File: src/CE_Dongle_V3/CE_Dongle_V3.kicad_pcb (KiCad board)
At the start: 4 copper layers, 44 x 44 mm, 106 parts, among them J1 USB_C_Receptacle_USB2.0_16P, J2 8P8C_LED_Shielded, J3 Conn_Coaxial, J4 Conn_02x05_Odd_Even, J5 Conn_01x02, Q1 AO3401A, Q2 AO3401A, Q3 BC817-40-7-F, Q4 BC817-40-7-F, Q5 BC817-40-7-F, U1 ESP32-C6, U10 TMUX1208QRSVRQ1, U11 TPS70950DBVR, U2 SP3485, U3 W25Q64JWUUIQ, U4 TPS54302DDCR, U5 PCF8574RGTR(UMW), U6 PCF8574RGTR(UMW), U7 TMUX1208QRSVRQ1, U8 TMUX1208QRSVRQ1, U9 TMUX1208QRSVRQ1, Y1 40MHz

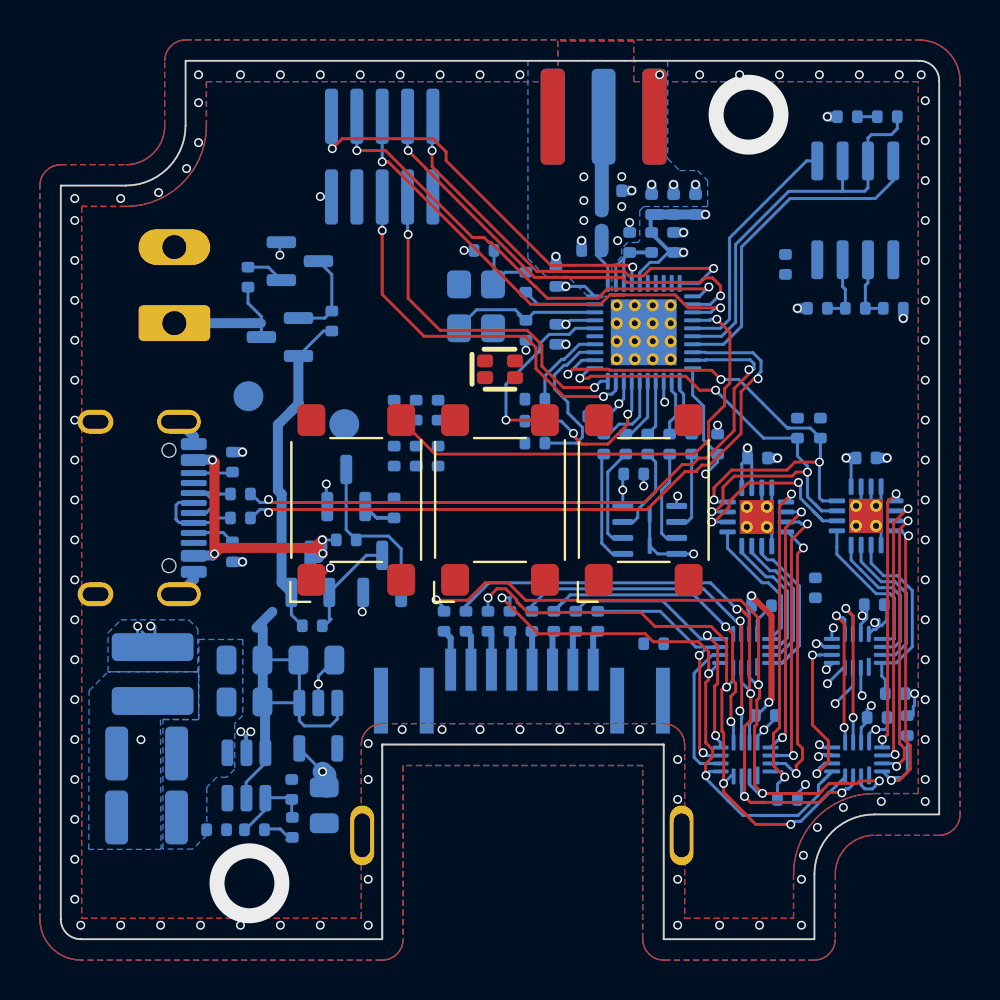
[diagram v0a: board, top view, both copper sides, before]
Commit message: layout cont. corrected some wrong net names
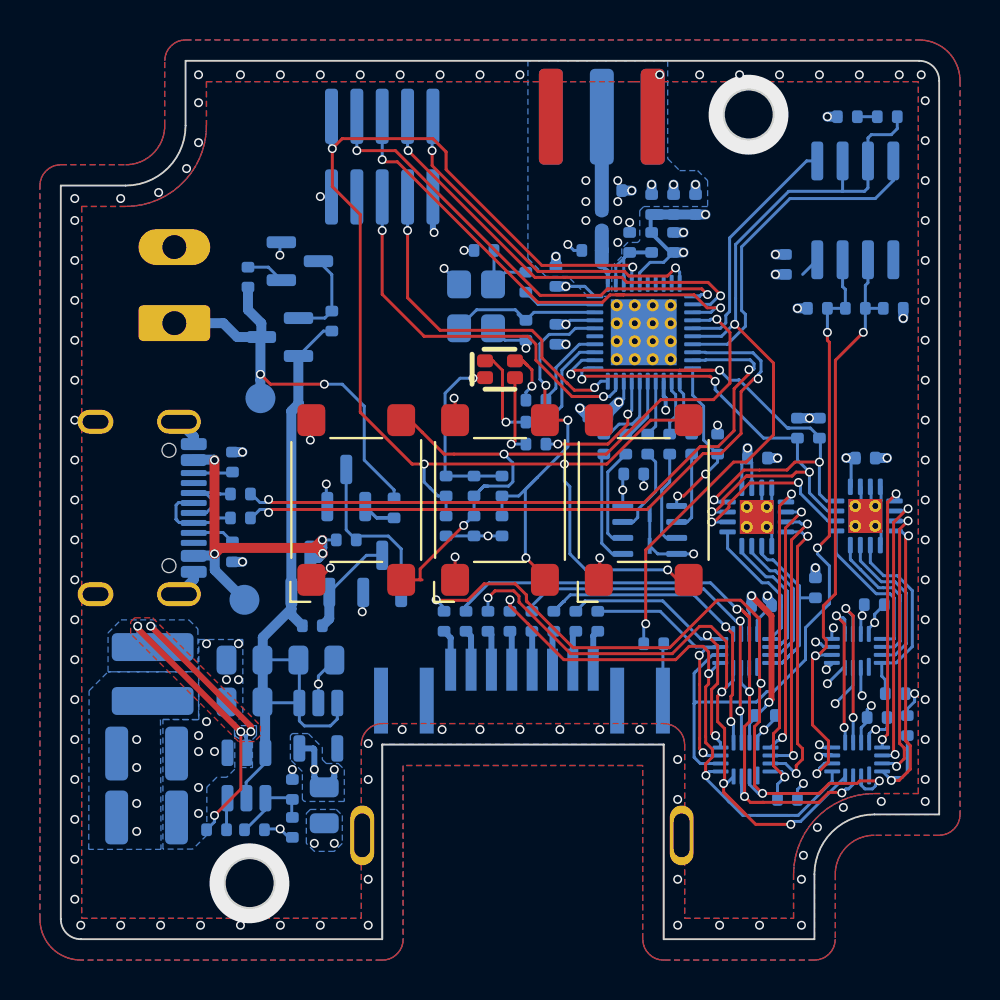
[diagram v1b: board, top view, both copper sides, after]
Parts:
- added REF**: 1551RFLGY, 7Sigma:1551RFLGY, F.Cu at (130.0, 127.0)
- moved TP2 10.1 mm to (117.2, 132.0)
- moved C24 6.62 mm to (130.1, 128.3), turned to -90 degrees
- moved C26 6.48 mm to (128.7, 128.3), turned to -90 degrees
- moved C25 6.36 mm to (127.3, 128.3), turned to -90 degrees
- moved R44 3.53 mm to (130.1, 126.3), turned to -90 degrees
- moved R22 3.26 mm to (128.7, 126.3), turned to -90 degrees
- moved R21 3.00 mm to (127.3, 126.3), turned to -90 degrees
- moved R24 1.15 mm to (131.8, 124.2)
- moved R23 1.05 mm to (131.8, 123.1)
- moved TP1 0.61 mm to (118.0, 121.9)
- moved J3 0.09 mm to (135.1, 107.8)
- moved R19 0.07 mm to (131.8, 122.0)
- moved R42 0.05 mm to (146.0, 123.4)
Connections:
- C6 pad 1: +3V3 -> 3VE
- R3 pad 1: +3V3 -> 3V3
- U1 pad 8: /MCU/LED_R -> unconnected-(U1-GPIO2-Pad8)
- U1 pad 9: /MCU/LED_G -> unconnected-(U1-GPIO3-Pad9)
- U2 pad 8: +3V3 -> 3V3
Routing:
- net /MCU/RST: track 20.7 -> 67.6 mm, vias 2 -> 5
- net 3V3: track 94.9 -> 139.8 mm, vias 8 -> 17
- net /MUX/OUT_B: track 10.8 -> 35.9 mm, vias 0 -> 2
- net /MUX/OUT_A: track 11.9 -> 32.6 mm, vias 2 -> 3
- net /TX_EN: track 20.4 -> 40.4 mm, vias 0 -> 2
- net /PWR/VEXT: track 7.39 -> 21.6 mm, vias 0 -> 2
- net GND: track 43.1 -> 55.6 mm, vias 128 -> 152
- net /MCU/BTTN: track 9.66 -> 20.6 mm, vias 1 -> 3
- net /MCU/GPIO8_BOOT: track 24.5 -> 34.0 mm, vias 1 -> 3
- net Net-(D7-RK): track 0.00 -> 4.74 mm, vias 0 -> 1
- net Net-(U4-SW): track 20.5 -> 24.9 mm, vias 4 -> 5
- net Net-(D7-BK): track 0.00 -> 4.13 mm, vias 0 -> 1
- net /MCU/LED_R: track 8.19 -> 4.96 mm
- net /MCU/MTMS: track 21.1 -> 18.0 mm
- net Net-(D7-GK): track 0.00 -> 3.07 mm, vias 0 -> 1
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- added copper zone on B.Cu, net 5V0
- added copper zone on F.Cu, net Net-(U4-SW)

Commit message: layout finished
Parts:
- removed R31, R32, R33, R34, R35, R36, R6, R7: 10R, 7Sigma:R_0402_1005Metric
- removed REF**: 1551RFLGY, 7Sigma:1551RFLGY
- added C18: 100pF, 7Sigma:C_0402_1005Metric, B.Cu at (131.7, 133.1)
- added C33: 100pF, 7Sigma:C_0402_1005Metric, B.Cu at (132.8, 133.1)
- added C34: 100pF, 7Sigma:C_0402_1005Metric, B.Cu at (133.9, 133.1)
- added C35: 100pF, 7Sigma:C_0402_1005Metric, B.Cu at (135.0, 133.1)
- added C36: 100pF, 7Sigma:C_0402_1005Metric, B.Cu at (130.6, 133.1)
- added C37: 100pF, 7Sigma:C_0402_1005Metric, B.Cu at (129.5, 133.1)
- added C38: 100pF, 7Sigma:C_0402_1005Metric, B.Cu at (128.4, 133.1)
- added C39: 100pF, 7Sigma:C_0402_1005Metric, B.Cu at (127.3, 133.1)
- added G1: 7Sigma Logo, 7Sigma:7Sigma_Logo, F.Cu at (123.9, 113.2)
- added G2: Hammond_1551RFLGY, 7Sigma:HAMMOND_1551RFLGY, F.Cu at (130.0, 127.0)
- added H1: MH_2.5mm_4mm_OD, 7Sigma:MountingHole_2.5mm_Pad_4mm, F.Cu at (117.5, 146.2)
- added H2: MH_2.5mm_4mm_OD, 7Sigma:MountingHole_2.5mm_Pad_4mm, F.Cu at (142.4, 107.7)
- added J6: WJ15EDGK-3.81-2P, 7Sigma:TerminalBlock_Plug_Invisible, B.Cu at (113.7, 116.1)
- R12, R13, R15, R16, R17: value 100R -> 22R
- R18: value 0R -> 120R
- SW_BOOT1, SW_RST1, SW_USR1: footprint 7Sigma:SW_SPST_6.0mm_6.0mm -> 7Sigma:SW-SMD_4P-L6.0-W6.0-P4.50-LS9.0-H4.3
- moved J3 0.51 mm to (135.1, 108.3)
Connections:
- C6 pad 1: 3VE -> 3V3
- J2 pad 1: /MUX/IN_1 -> /MUX/MUX_IN_1
- J2 pad 2: /MUX/IN_2 -> /MUX/MUX_IN_2
- J2 pad 3: /MUX/IN_3 -> /MUX/MUX_IN_3
- J2 pad 4: /MUX/IN_4 -> /MUX/MUX_IN_4
- J2 pad 5: /MUX/IN_5 -> /MUX/MUX_IN_5
- J2 pad 6: /MUX/IN_6 -> /MUX/MUX_IN_6
- J2 pad 7: /MUX/IN_7 -> /MUX/MUX_IN_7
- J2 pad 8: /MUX/IN_8 -> /MUX/MUX_IN_8
- SW_BOOT1 pad 2: /MCU/GPIO8_BOOT -> GND
- SW_RST1 pad 2: /MCU/RST -> GND
- SW_USR1 pad 2: /MCU/BTTN -> GND
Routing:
- net GND: track 55.6 -> 62.5 mm, vias 152 -> 155
- net /MUX/MUX_IN_5: track 32.9 -> 35.7 mm, vias 4 -> 6
- net /MUX/IN_1: track 2.06 -> 0.00 mm
- net /MUX/IN_2: track 2.03 -> 0.00 mm
- net /MUX/IN_8: track 2.02 -> 0.00 mm
- net /MUX/IN_3: track 2.00 -> 0.00 mm
- net /MUX/IN_7: track 1.99 -> 0.00 mm
- net /MUX/MUX_IN_2: track 43.2 -> 45.1 mm
- net /MUX/IN_4: track 1.96 -> 0.00 mm
- net /MUX/IN_6: track 1.95 -> 0.00 mm
- net /MUX/IN_5: track 1.93 -> 0.00 mm
- net /MCU/RST: track 67.6 -> 65.8 mm
- net /MCU/I2C_SDA: track 28.0 -> 26.2 mm
- net /MUX/MUX_IN_8: track 28.2 -> 29.9 mm
- net /MUX/MUX_IN_7: track 28.3 -> 29.7 mm
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- added copper zone on B.Cu, net Net-(C10-Pad1)
- added copper zone on B.Cu, net Net-(U1-ANT)
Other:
- outline, holes or cut-outs redrawn
- board text added: "CE_DONGLE_V3"

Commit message: schematic update before production
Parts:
- removed J6: WJ15EDGK-3.81-2P, 7Sigma:TerminalBlock_Plug_Invisible
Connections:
- net /MUX/MUX_IN_1 renamed /MUX/IN_1
- net /MUX/MUX_IN_2 renamed /MUX/IN_2
- net /MUX/MUX_IN_3 renamed /MUX/IN_3
- net /MUX/MUX_IN_4 renamed /MUX/IN_4
- net /MUX/MUX_IN_5 renamed /MUX/IN_5
- net /MUX/MUX_IN_6 renamed /MUX/IN_6
- net /MUX/MUX_IN_7 renamed /MUX/IN_7
- net /MUX/MUX_IN_8 renamed /MUX/IN_8
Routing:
- net GND: vias 155 -> 163
